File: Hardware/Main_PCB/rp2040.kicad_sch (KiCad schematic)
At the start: 28 parts, among them P301 USB_C_Plug_USB2.0, SW301 TL3342F160QG_TR, SW302 TL3342F160QG_TR, U301 RP2040, U302 W25Q128JVS, Y301 12Mhz

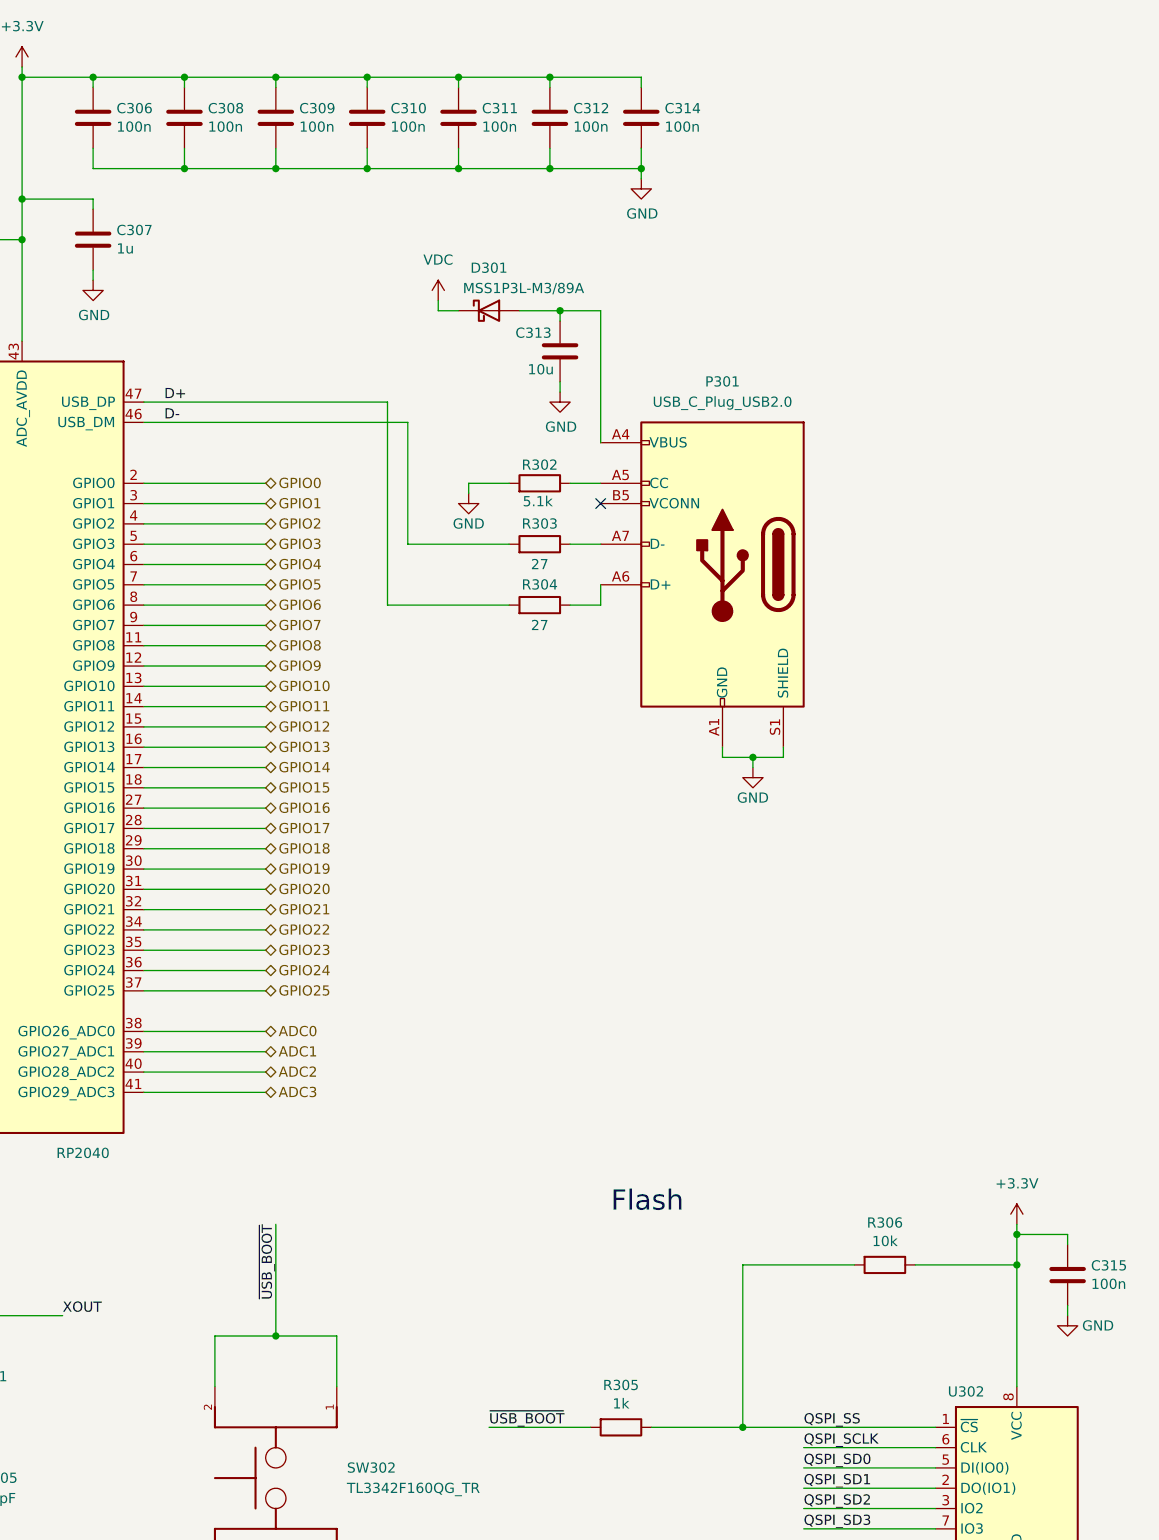
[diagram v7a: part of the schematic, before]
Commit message: Updated the PCB with new USB-C
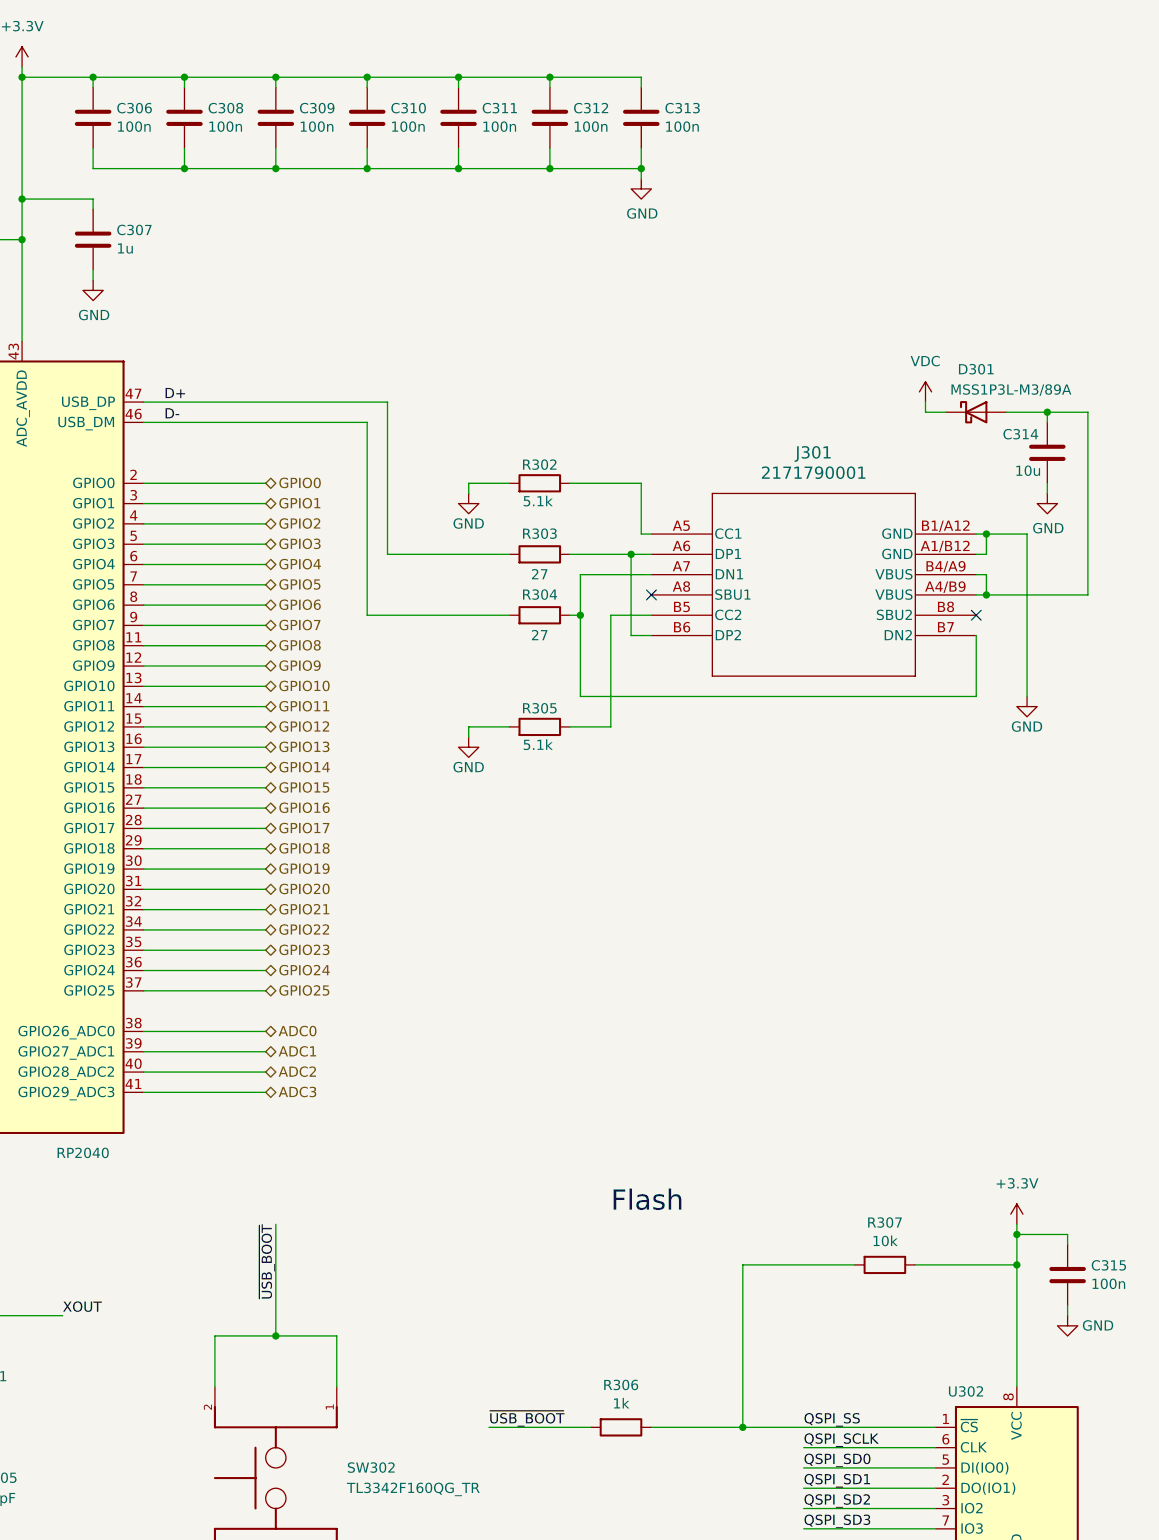
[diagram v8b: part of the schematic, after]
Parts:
- removed P301: USB_C_Plug_USB2.0, MainPCB:CUI_UJC-HP-3-SMT-TR, symbol Connector:USB_C_Plug_USB2.0
- added J301: 2171790001, MainPCB:2171790001_MOL, symbol MainPCB_Sym_lib:2171790001
- added R305: 5.1k, Resistor_SMD:R_0603_1608Metric_Pad0.98x0.95mm_HandSolder, symbol Device:R
- renumbered C314 to C313, C313 to C314, R304 to R303, R303 to R304, R305 to R306, R306 to R307
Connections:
- net GND: now also J301.A1/B12 (GND), J301.B1/A12 (GND), R305.2
- net at R304.1: now also J301.A7 (DN1), J301.B7 (DN2)
- net at C314.1, D301.2 (A): now also J301.A4/B9 (VBUS), J301.B4/A9 (VBUS)
- net at R302.1: now also J301.A5 (CC1)
- net at R303.1: now also J301.A6 (DP1), J301.B6 (DP2)
- new net: J301.B5 (CC2), R305.1
- no-connect marks 5 -> 6
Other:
- moved on the sheet: C314, D301, R303, R304
